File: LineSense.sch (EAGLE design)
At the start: 45 parts, among them IC1 NJM2904M-TE1, IC2 NE555D, J1 1744426-4, Q1 SFH_3410-1_2-Z, Q2 2SC2712-GR,LF, Q3 2SC2712-GR,LF, Q5 2SC2712-GR,LF, Q6 2SC2712-GR,LF

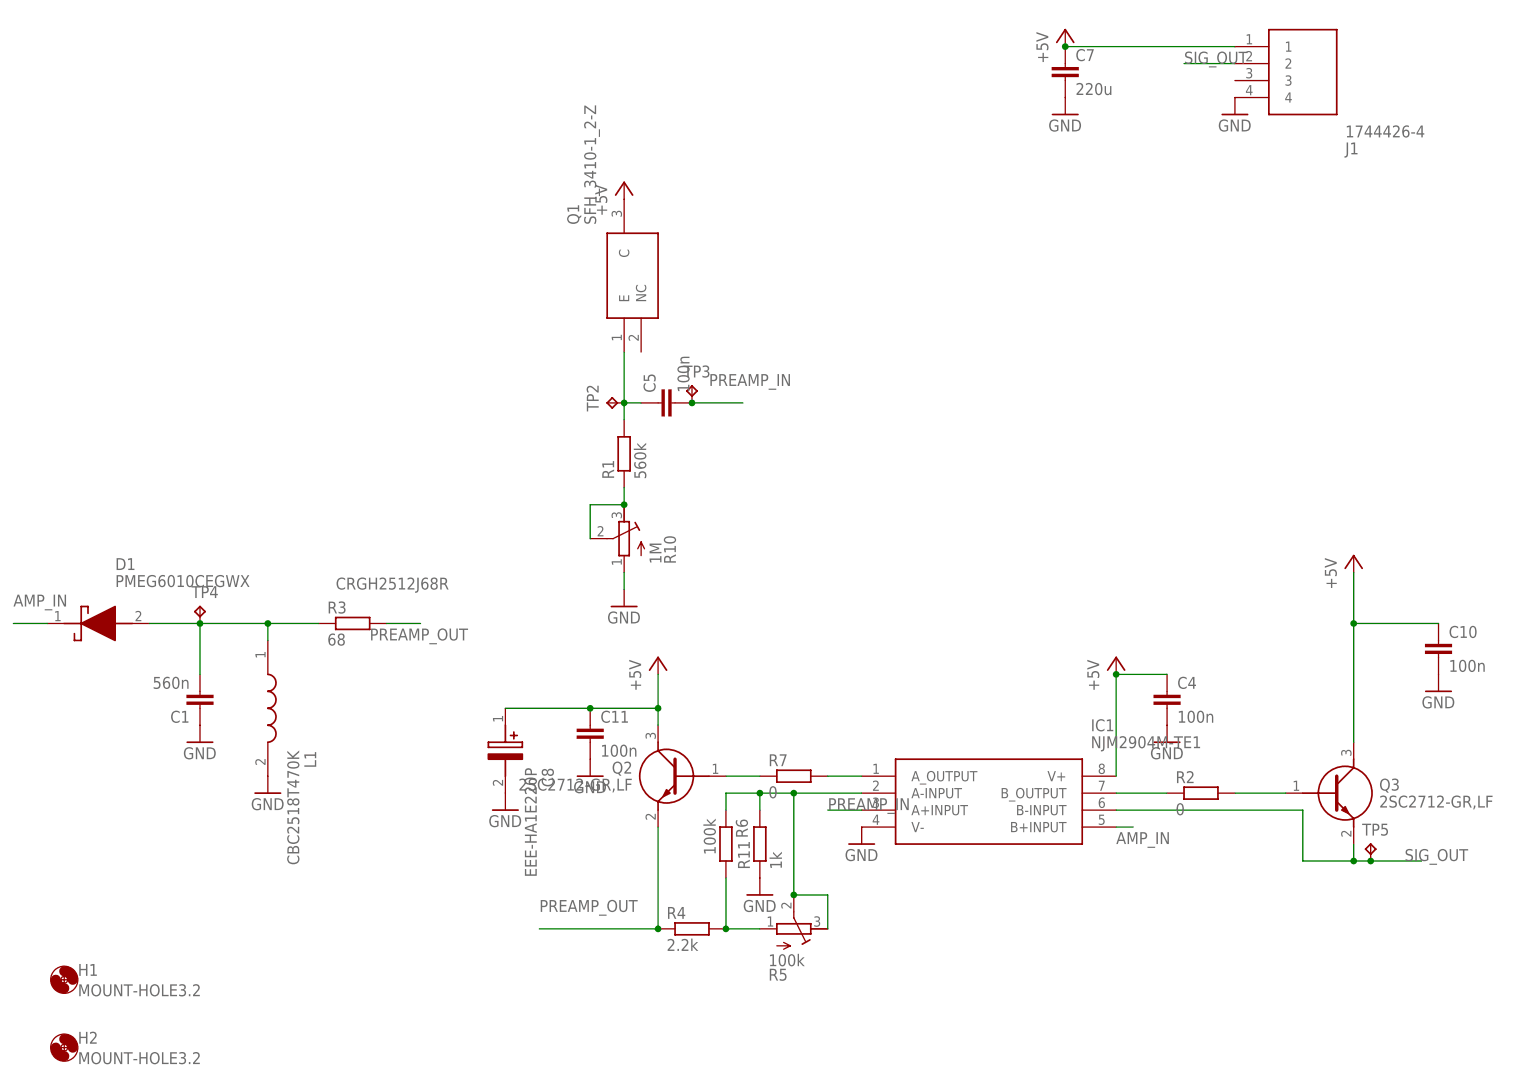
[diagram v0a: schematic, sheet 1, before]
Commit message: Revert "v1.2"
This reverts commit 20100e136a2bdf049fa62e188f43b768e8603774.
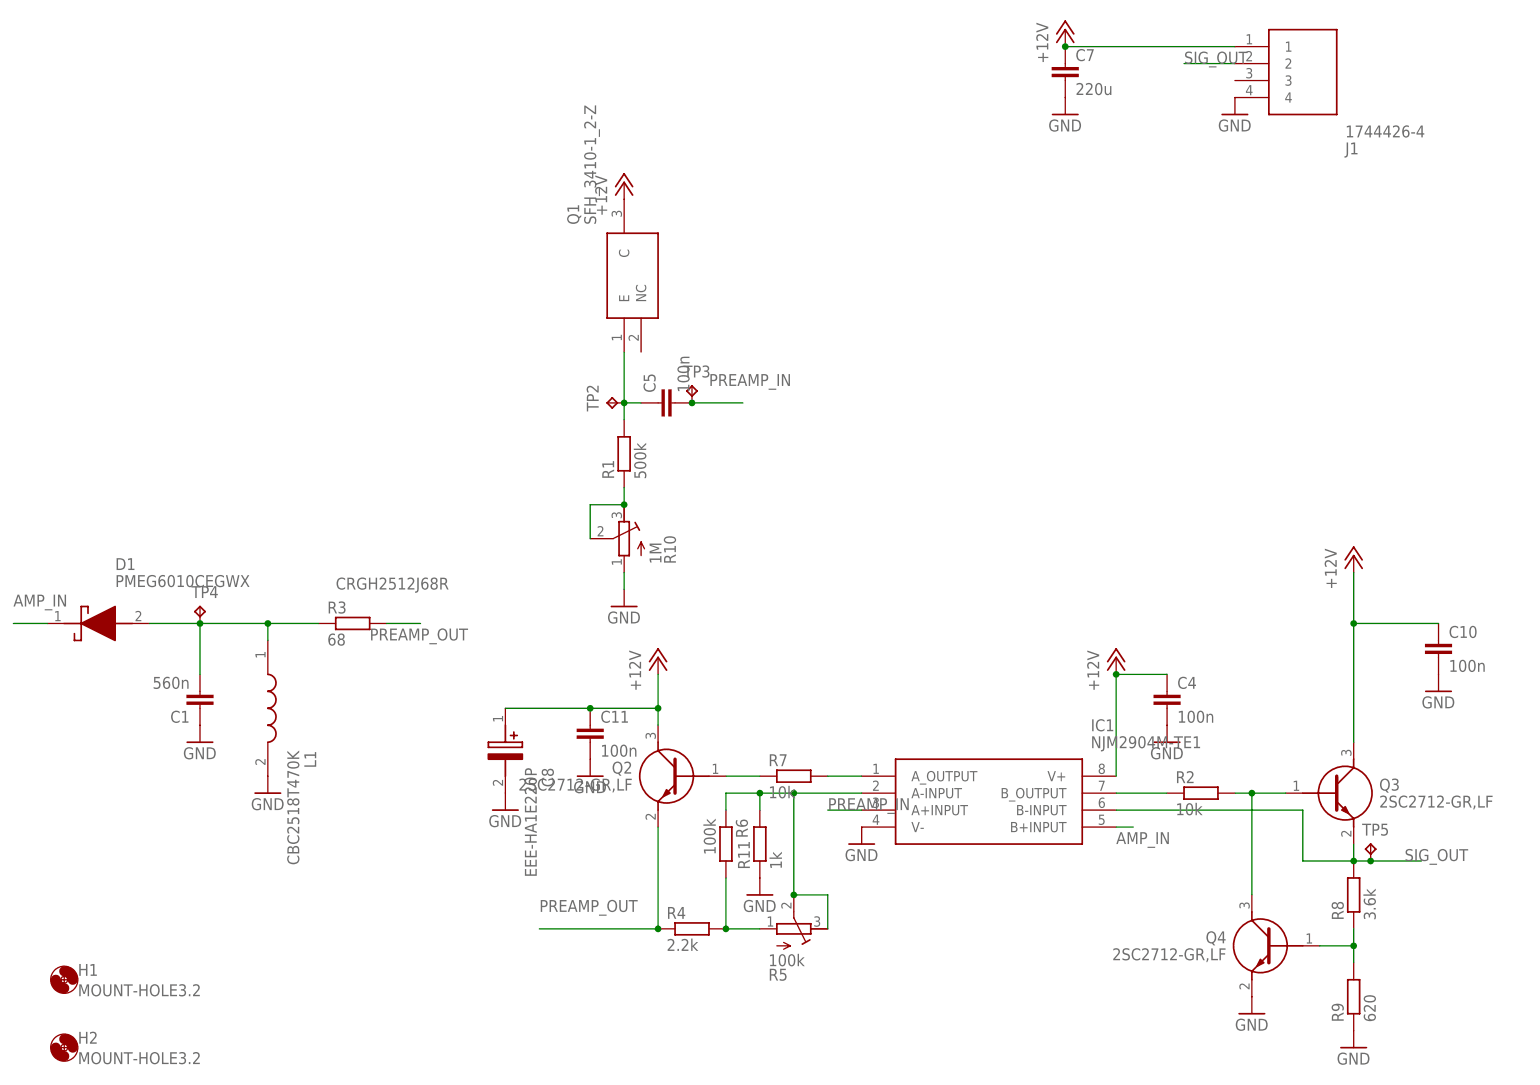
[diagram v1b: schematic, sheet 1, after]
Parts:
- added Q4: 2SC2712-GR,LF, SamacSys_Parts:2SC2712-GR,LF
- added R8: 3.6k, rcl:R-EU_R0603
- added R9: 620, rcl:R-EU_R0603
- R1: value 560k -> 500k
- R13: value 4.7k -> 7.5k
- R2, R7: value 0 -> 10k
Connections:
- net +5V renamed +12V
- new net N$10: Q4.B, R8.1, R9.2
- net GND: now also Q4.E, R9.1
- net N$8: now also Q4.C
- net SIG_OUT: now also R8.2
